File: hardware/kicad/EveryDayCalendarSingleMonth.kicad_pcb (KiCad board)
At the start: 2 copper layers, 100 x 100 mm, 142 parts, among them J1_ONE_WIRE1 Conn_01x03, J2_POWER_IN1 Conn_01x02, J3_PROGRAMING_PIN1 Conn_01x06, Q1_PROGRAMING1 PN2222A, Q2_PROGRAMING1 PN2222A, U1 74AHC1G125

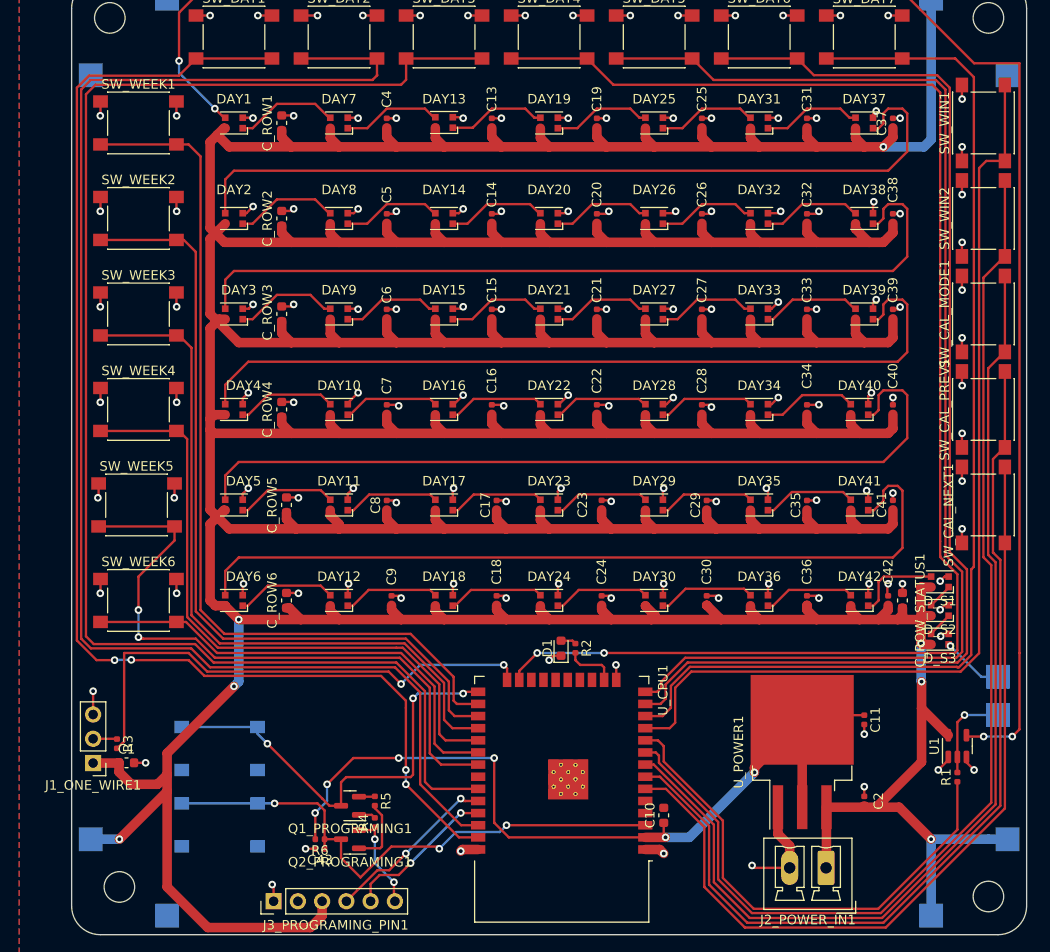
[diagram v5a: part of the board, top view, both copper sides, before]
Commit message: Updated silkscreen
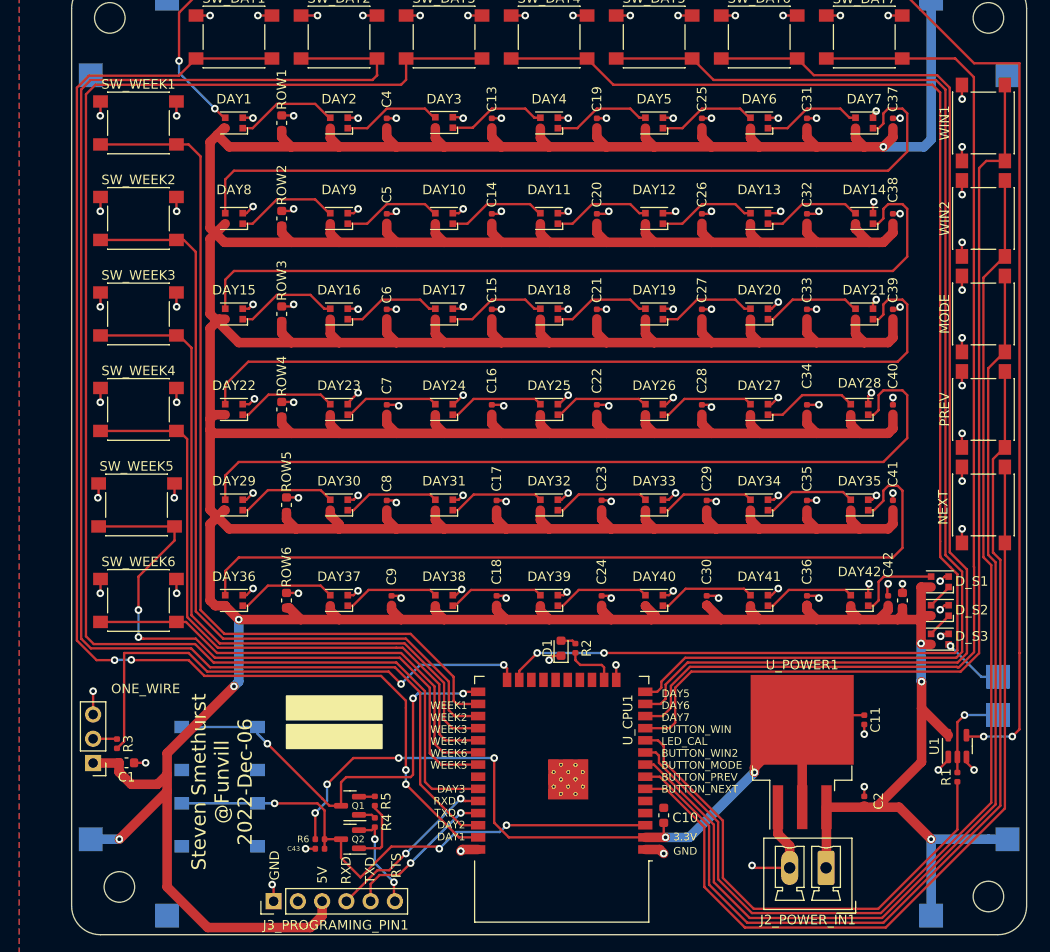
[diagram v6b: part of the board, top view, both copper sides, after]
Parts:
- renumbered TP_BOTTOM_5V1 to 5V, TP_RIGHT_5V1 to 5V, TP_LEFT_5V1 to 5V, TP_TOP_5V1 to 5V, DAY14 to DAY10, DAY20 to DAY11, DAY26 to DAY12, DAY32 to DAY13, DAY38 to DAY14, DAY3 to DAY15, DAY9 to DAY16, DAY15 to DAY17, DAY21 to DAY18, DAY27 to DAY19, DAY7 to DAY2, DAY33 to DAY20, DAY39 to DAY21, DAY4 to DAY22, DAY10 to DAY23, DAY16 to DAY24, DAY22 to DAY25, DAY28 to DAY26, DAY34 to DAY27, DAY40 to DAY28, DAY5 to DAY29, DAY13 to DAY3, DAY11 to DAY30, DAY17 to DAY31, DAY23 to DAY32, DAY29 to DAY33, DAY35 to DAY34, DAY41 to DAY35, DAY6 to DAY36, DAY12 to DAY37, DAY18 to DAY38, DAY24 to DAY39, DAY19 to DAY4, DAY30 to DAY40, DAY36 to DAY41, DAY25 to DAY5, DAY31 to DAY6, DAY37 to DAY7, DAY2 to DAY8, DAY8 to DAY9, TP_RIGHT_GND1 to GND, TP_TOP_GND1 to GND, TP_BOTTOM_GND1 to GND, TP_LEFT_GND1 to GND, TP_LEDLINK_IN1 to LED_IN, TP_LEDLINK_OUT1 to LED_OUT, SW_CAL_MODE1 to MODE, SW_CAL_NEXT1 to NEXT, J1_ONE_WIRE1 to ONE_WIRE, SW_CAL_PREV1 to PREV, Q1_PROGRAMING1 to Q1, Q2_PROGRAMING1 to Q2, C_ROW1 to ROW1, C_ROW2 to ROW2, C_ROW3 to ROW3, C_ROW4 to ROW4, C_ROW5 to ROW5, C_ROW6 to ROW6, SW_WIN1 to WIN1, SW_WIN2 to WIN2
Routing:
- net GND: track 187.2 -> 188.1 mm
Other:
- board text added: "3.3V"
- board text added: "5V"
- board text added: "BUTTON_MODE"
- board text added: "BUTTON_NEXT"
- board text added: "BUTTON_PREV"
- board text added: "BUTTON_WIN"
- board text added: "BUTTON_WIN2"
- board text added: "DAY1"
- board text added: "DAY2"
- board text added: "DAY3"
- board text added: "DAY5"
- board text added: "DAY6"
- board text added: "DAY7"
- board text added: "GND"
- board text added: "GPIO0"
- board text added: "LED_CAL"
- board text added: "RESET"
- board text added: "RTS"
- board text added: "RXD"
- board text added: "Steven Smethurst @Funvill 2022-Dec-06"
- board text added: "TXD"
- board text added: "WEEK1"
- board text added: "WEEK2"
- board text added: "WEEK3"
- board text added: "WEEK4"
- board text added: "WEEK5"
- board text added: "WEEK6"

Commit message: Updated the schematic from PCB layout with updated silkscreen
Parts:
- renumbered 5V to 5V1, 5V to 5V2, 5V to 5V3, 5V to 5V4, GND to GND1, GND to GND2, GND to GND3, GND to GND4, LED_IN to LED_IN1, LED_OUT to LED_OUT1, MODE to MODE1, NEXT to NEXT1, ONE_WIRE to ONE_WIRE1, PREV to PREV1

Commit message: Fussing with the tracks, no real change
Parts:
- added CAL_NEXT1: TestPoint, TestPoint:TestPoint_Pad_2.5x2.5mm, B.Cu at (148.0, 95.0)
- added CAL_PREV1: TestPoint, TestPoint:TestPoint_Pad_2.5x2.5mm, B.Cu at (148.0, 85.0)
- added MODE1: TestPoint, TestPoint:TestPoint_Pad_2.5x2.5mm, B.Cu at (148.0, 75.0)
- added WIN1: TestPoint, TestPoint:TestPoint_Pad_2.5x2.5mm, B.Cu at (148.0, 55.0)
- added WIN2: TestPoint, TestPoint:TestPoint_Pad_2.5x2.5mm, B.Cu at (148.0, 65.0)
- moved R3 7.54 mm to (55.5, 112.5), turned to 90 degrees
- moved C1 2.37 mm to (55.0, 124.2), turned to -90 degrees
- moved J2_POWER_IN1 1.75 mm to (129.0, 134.8)
- moved C2 1.25 mm to (133.0, 127.2), turned to -90 degrees
- moved LED_IN1 1.00 mm to (148.0, 117.0)
- moved LED_OUT1 1.00 mm to (148.0, 113.0)
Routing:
- net /PIN_ONE_WIRE: track 53.9 -> 45.0 mm
- net Net-(ONE_WIRE1-Pad2): track 2.51 -> 9.62 mm
- net +3.3V: track 87.4 -> 83.1 mm, vias 6 -> 4
- net /DAY4: track 153.3 -> 157.1 mm, vias 2 -> 0
- net /BUTTON_WIN1: track 102.1 -> 104.3 mm, vias 0 -> 1
- net /DAY5: track 130.7 -> 132.8 mm
- net /DAY6: track 121.9 -> 124.0 mm
- net /DAY7: track 115.1 -> 117.1 mm
- net /RXD: track 18.4 -> 20.0 mm
- net +5V: track 828.9 -> 827.5 mm
- net /GPIO0: track 46.0 -> 47.2 mm
- net Net-(LED_IN1-Pad1): track 9.83 -> 10.8 mm
- net Net-(D_S3-Pad1): track 6.58 -> 7.58 mm
- net GND: track 188.1 -> 188.9 mm
- net /BUTTON_WIN2: vias 0 -> 1
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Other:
- board text added: "GPIO02"
- board text added: "JLCJLCJLCJLC"
